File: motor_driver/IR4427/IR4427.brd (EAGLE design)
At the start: 34 x 37 mm, 33 parts, among them IC1 IR4427, IC2 IR4427, IC3 IR4427, IC5 ACS712-LC, Q1 IRF7389, Q2 IRF7389, Q3 IRF7389

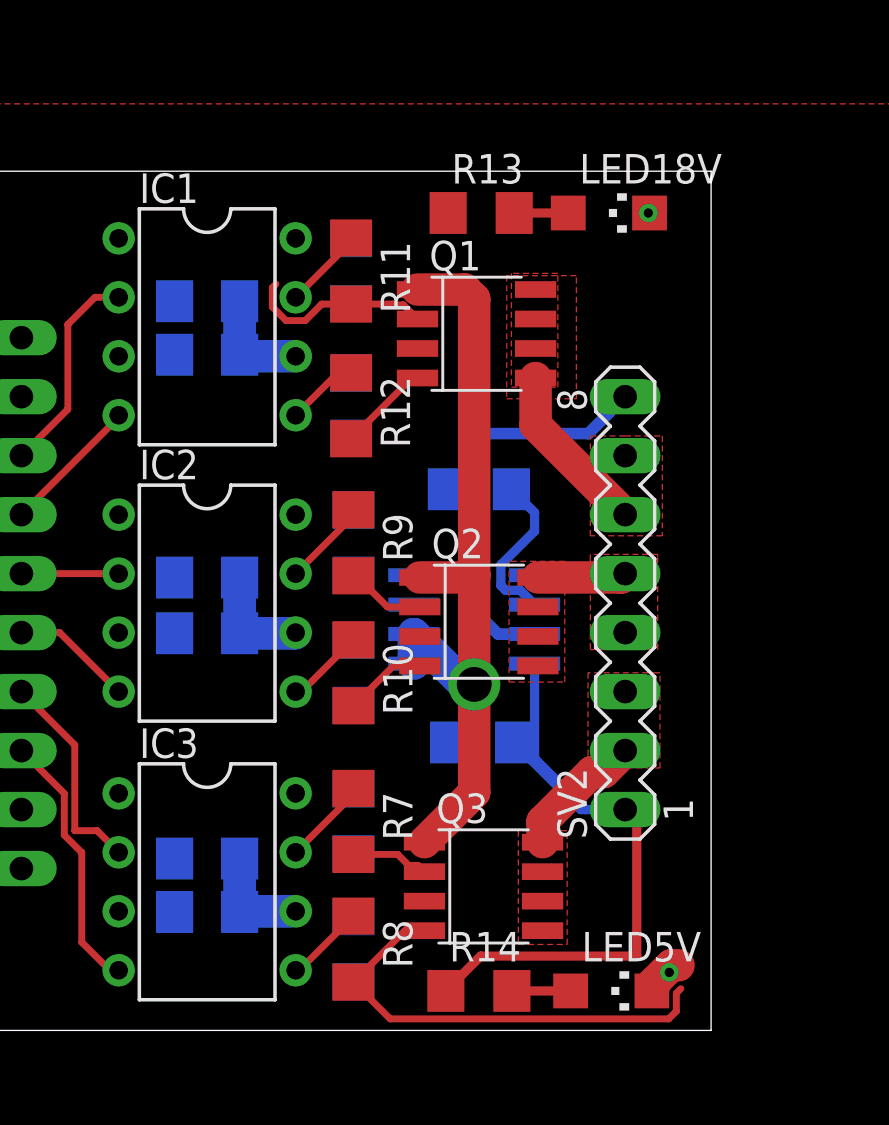
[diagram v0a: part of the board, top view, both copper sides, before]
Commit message: eagle 7 compatible
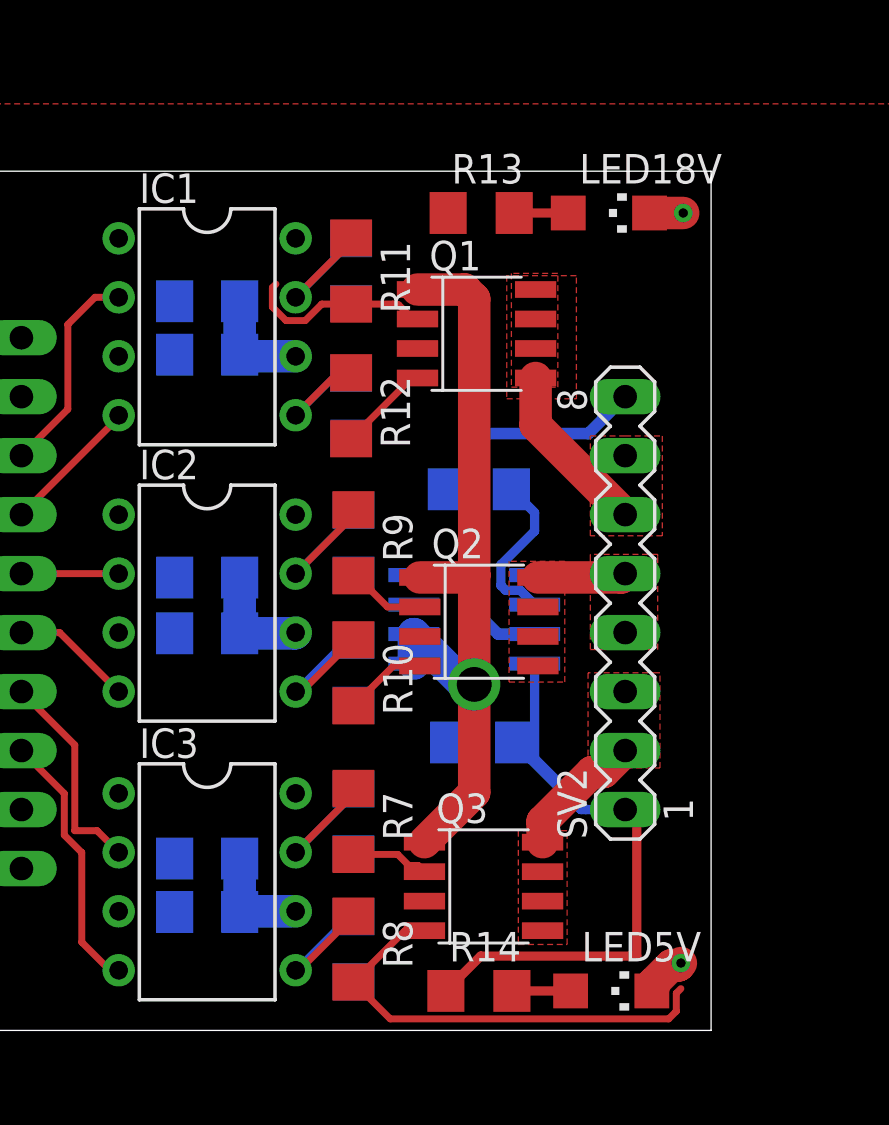
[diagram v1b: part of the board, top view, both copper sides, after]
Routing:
- net OUT_3A: track 3.78 -> 7.54 mm
- net OUT_2A: track 3.78 -> 7.54 mm
- net OUT_1A: track 3.54 -> 7.06 mm
- net OUT_3B: track 3.46 -> 6.90 mm
- net OUT_2B: track 3.41 -> 6.82 mm
- net OUT_1B: track 3.15 -> 6.29 mm
- net GND: track 1.76 -> 3.35 mm
